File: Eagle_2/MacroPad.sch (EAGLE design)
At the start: 40 parts, among them SW00 SWITCH-SMD-EVQP-P2602W, SW01 KEYSWITCH-PLAIN-MX-1U, SW02 KEYSWITCH-PLAIN-MX-1U, SW03 KEYSWITCH-PLAIN-MX-1U, SW04 KEYSWITCH-PLAIN-MX-1U, SW05 KEYSWITCH-PLAIN-MX-1U, SW06 KEYSWITCH-PLAIN-MX-1U, SW07 KEYSWITCH-PLAIN-MX-1U, SW08 KEYSWITCH-PLAIN-MX-1U, SW09 KEYSWITCH-PLAIN-MX-1U, SW10 KEYSWITCH-PLAIN-MX-1U, SW11 KEYSWITCH-PLAIN-MX-1U, SW12 KEYSWITCH-PLAIN-MX-1U

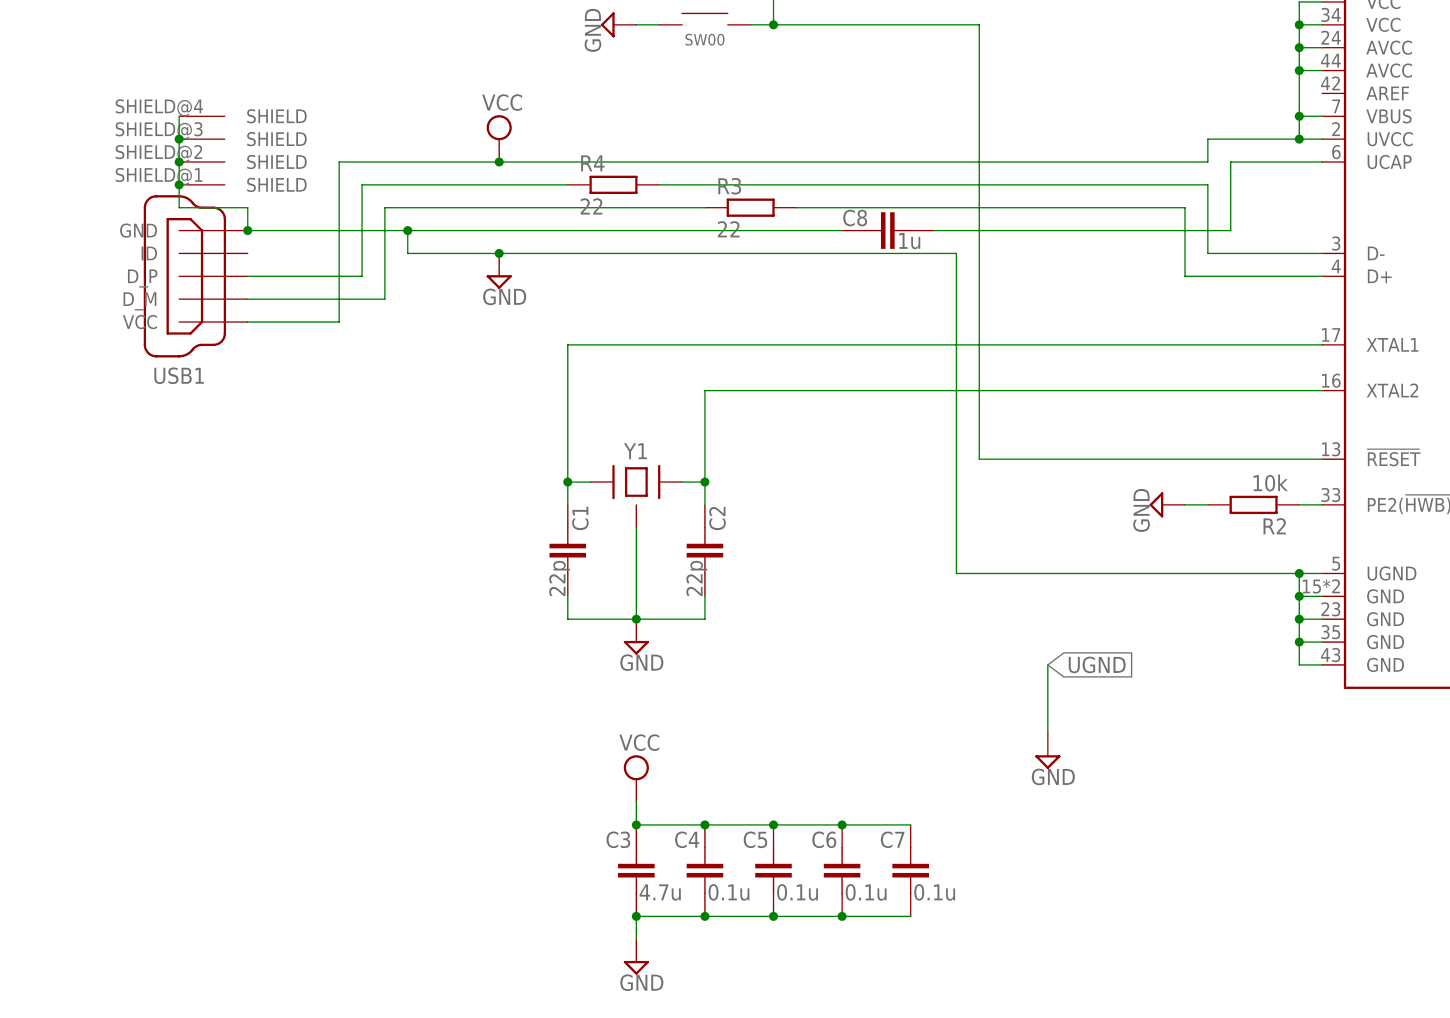
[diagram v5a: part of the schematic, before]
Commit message: Redone schematic with smaller capacitors, fixed decoupling capacitors, and adjusted trace sizes
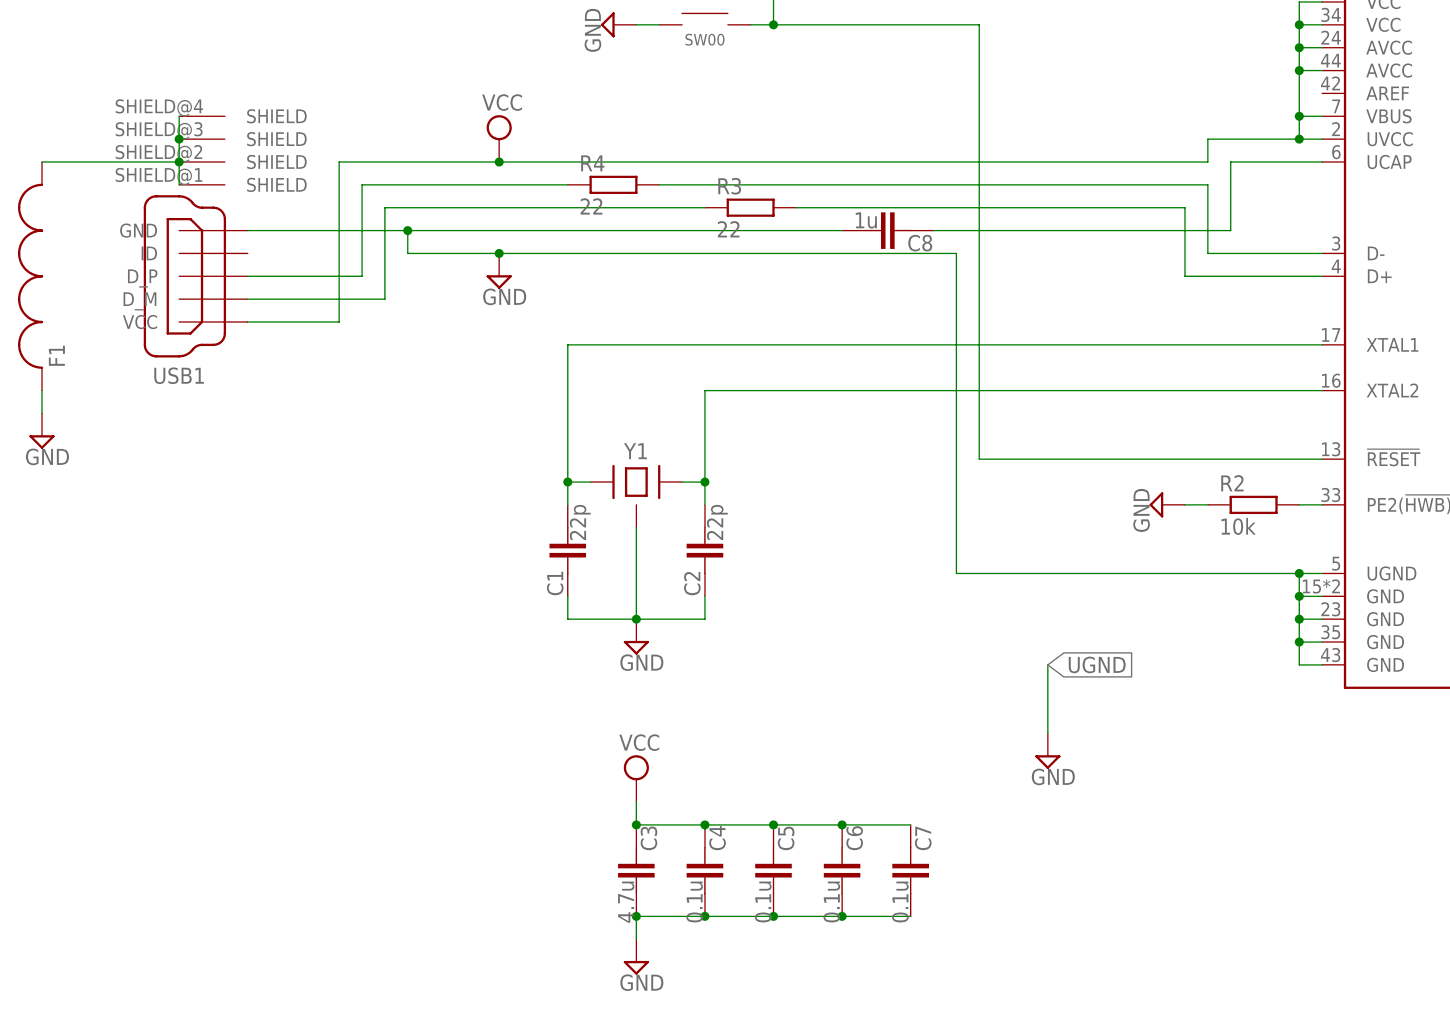
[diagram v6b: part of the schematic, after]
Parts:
- added F1: (no value), USB:FERRITE-0805
- C1, C2, C3, C4, C5, C6, C7, C8: device Components:CAPACITOR-C0805 -> Components:CAPACITOR-0603
- R1, R2, R3, R4: device Components:RESISTOR-0805 -> Components:RESISTOR-0603
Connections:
- new net GND: F1.P$1
- new net N$11: F1.P$2, USB1.SHIELD@1, USB1.SHIELD@2, USB1.SHIELD@3, USB1.SHIELD@4
- net N$1: now also C2.2; no longer C2.1
- net N$2: now also C1.2; no longer C1.1
- net N$4: now also R2.2; no longer R2.1
- net UCAP: now also C8.1; no longer C8.2
- net UGND: now also C1.1, C2.1, C3.2, C4.2, C5.2, C6.2, C7.2, C8.2, R2.1; no longer C1.2, C2.2, C3.1, C4.1, C5.1, C6.1, C7.1, C8.1, R2.2, USB1.SHIELD@1, USB1.SHIELD@2, USB1.SHIELD@3, USB1.SHIELD@4
- net VCC: now also C3.1, C4.1, C5.1, C6.1, C7.1; no longer C3.2, C4.2, C5.2, C6.2, C7.2
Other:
- moved on the sheet: C1, C2, C3, C4, C5, C6, C7, C8, R2

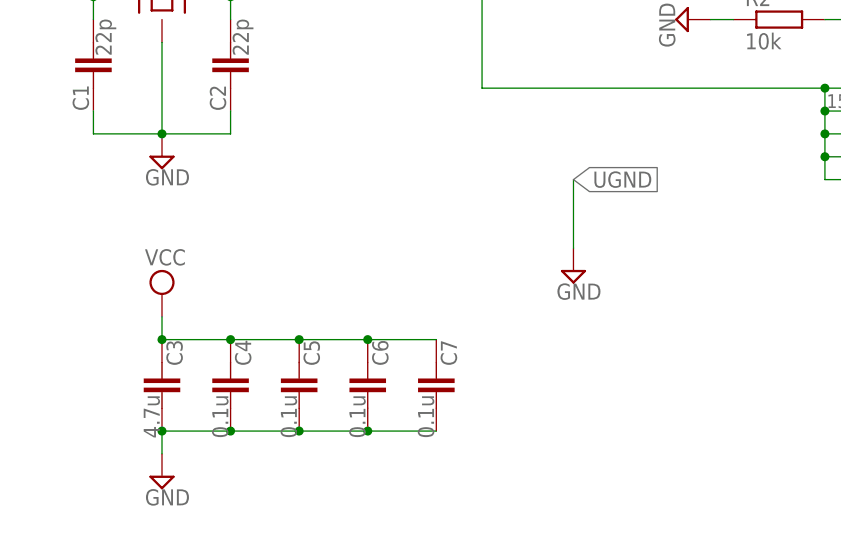
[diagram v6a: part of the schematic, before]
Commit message: Add top and bottom ground plane and merge gnd and ugnd
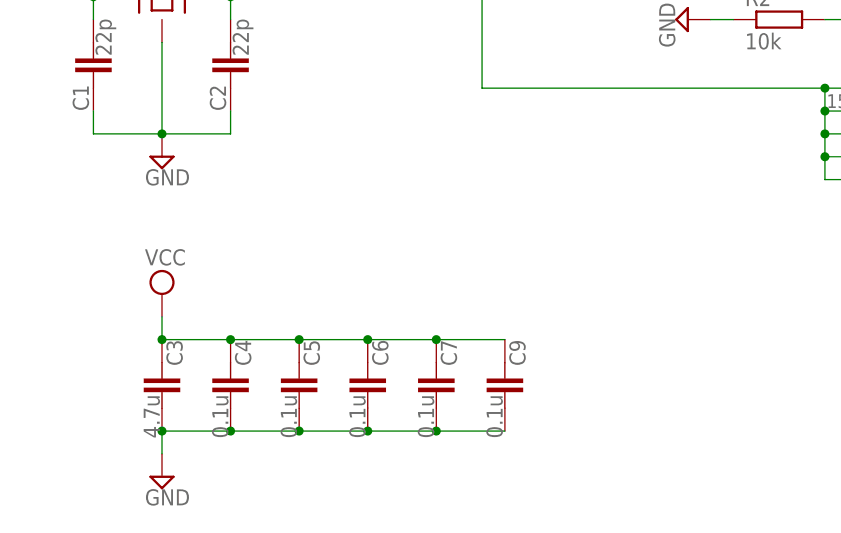
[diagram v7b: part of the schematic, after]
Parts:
- added C9: 0.1u, Components:CAPACITOR-0603
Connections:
- removed net UGND: C1.1, C2.1, C3.2, C4.2, C5.2, C6.2, C7.2, C8.2, R2.1, SW00.1, U$1.GND@15, U$1.GND@23, U$1.GND@35, U$1.GND@43, U$1.UGND, USB1.GND, Y1.GND
- net GND: now also C1.1, C2.1, C3.2, C4.2, C5.2, C6.2, C7.2, C8.2, C9.2, R2.1, SW00.1, U$1.GND@15, U$1.GND@23, U$1.GND@35, U$1.GND@43, U$1.UGND, USB1.GND, Y1.GND
- net VCC: now also C9.1

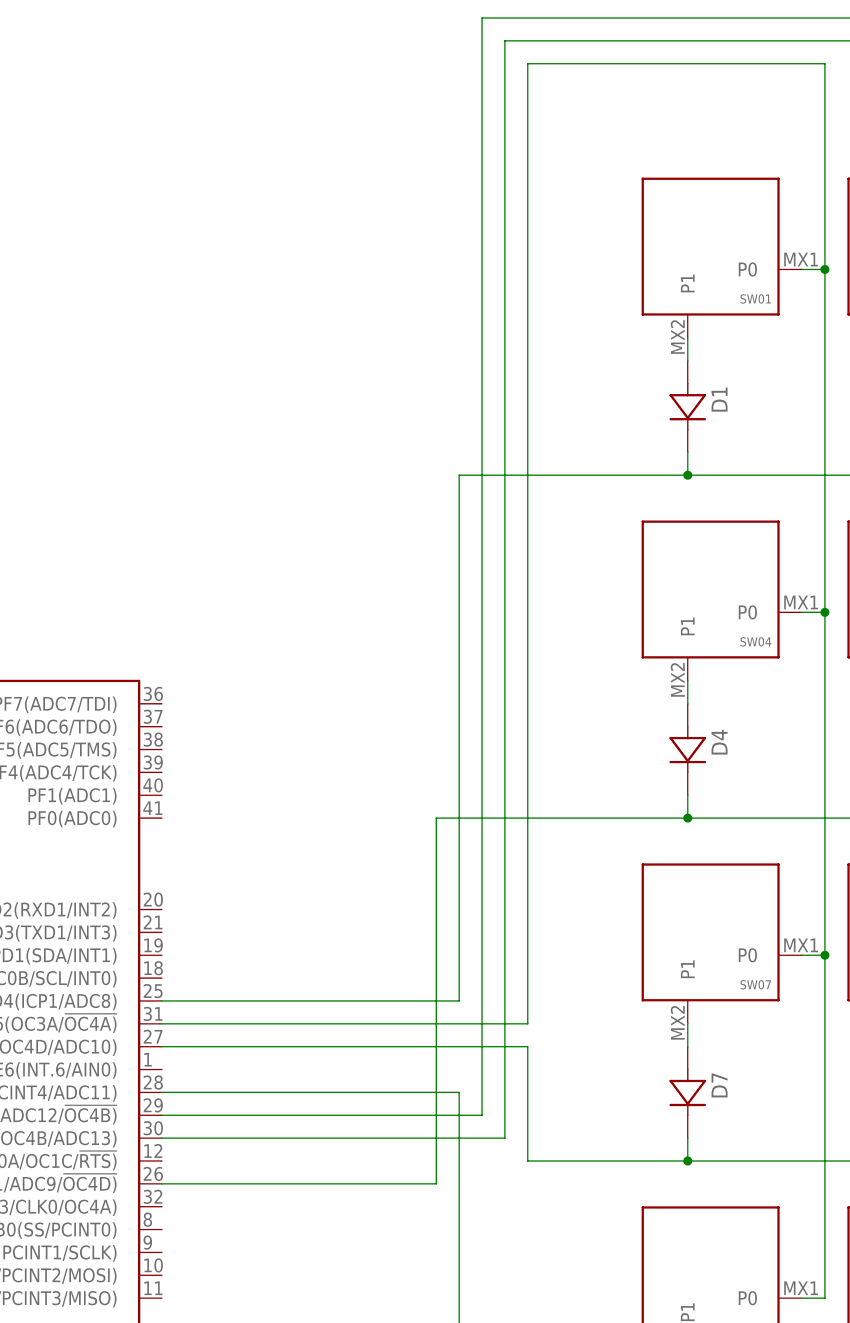
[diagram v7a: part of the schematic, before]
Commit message: Update layout with appropriate spacing between switches (100mil border)
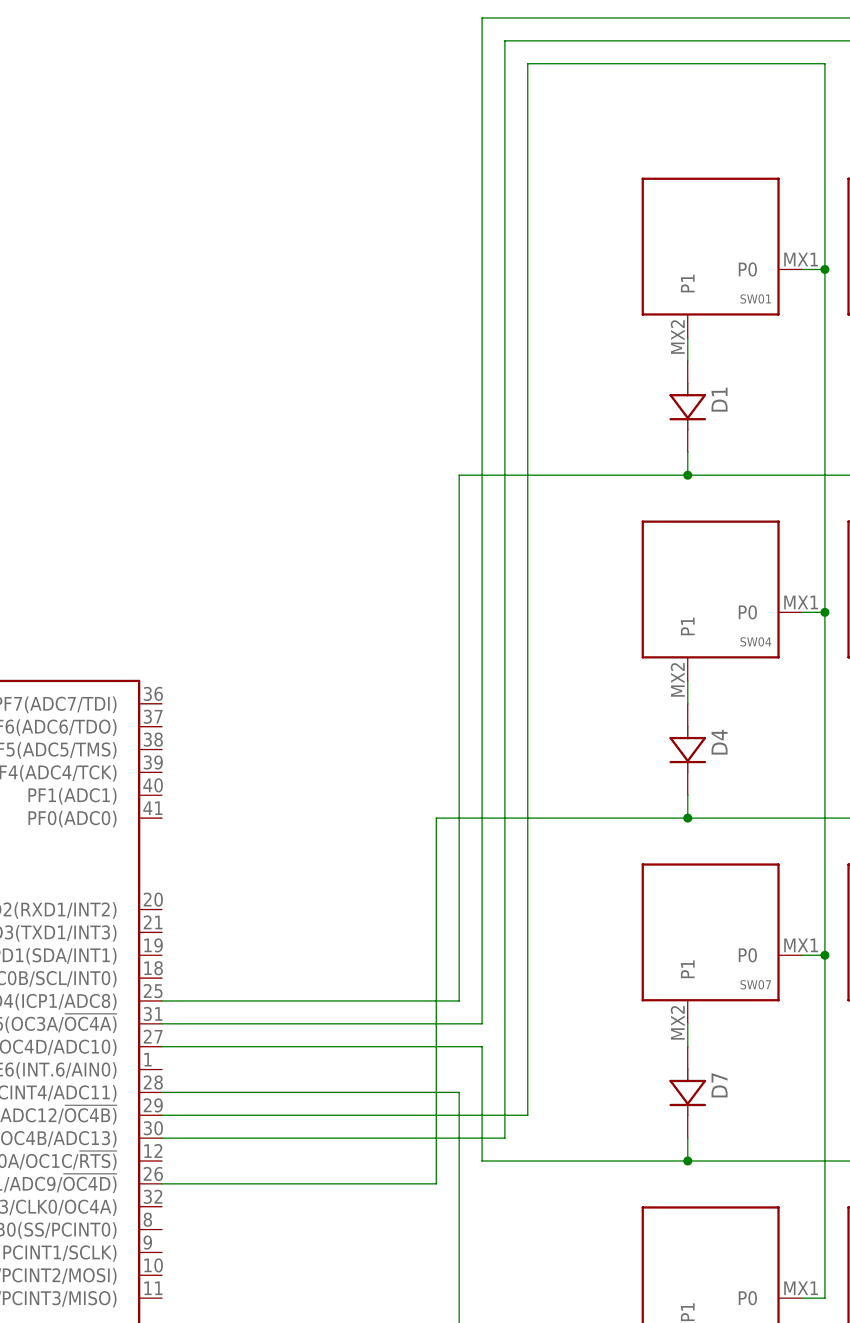
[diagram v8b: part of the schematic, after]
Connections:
- net N$10: now also U$1.PB5(PCINT5/OC1A/ADC12/!OC4B); no longer U$1.PC6(OC3A/!OC4A)
- net N$16: now also U$1.PC6(OC3A/!OC4A); no longer U$1.PB5(PCINT5/OC1A/ADC12/!OC4B)
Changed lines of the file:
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@@
 <junction x="228.6" y="73.66"/>
 <wire x1="195.58" y1="172.72" x2="228.6" y2="172.72" width="0.1524" layer="91"/>
-<pinref part="U$1" gate="G$1" pin="PC6(OC3A/!OC4A)"/>
-<wire x1="154.94" y1="66.04" x2="195.58" y2="66.04" width="0.1524" layer="91"/>
-<wire x1="195.58" y1="66.04" x2="195.58" y2="172.72" width="0.1524" layer="91"/>
+<wire x1="195.58" y1="55.88" x2="195.58" y2="172.72" width="0.1524" layer="91"/>
+<pinref part="U$1" gate="G$1" pin="PB5(PCINT5/OC1A/ADC12/!OC4B)"/>
+<wire x1="154.94" y1="55.88" x2="195.58" y2="55.88" width="0.1524" layer="91"/>
 </segment>
 </net>
@@
 <junction x="274.32" y="73.66"/>
 <wire x1="190.5" y1="177.8" x2="274.32" y2="177.8" width="0.1524" layer="91"/>
-<wire x1="190.5" y1="177.8" x2="190.5" y2="55.88" width="0.1524" layer="91"/>
-<pinref part="U$1" gate="G$1" pin="PB5(PCINT5/OC1A/ADC12/!OC4B)"/>
-<wire x1="190.5" y1="55.88" x2="154.94" y2="55.88" width="0.1524" layer="91"/>
+<wire x1="190.5" y1="177.8" x2="190.5" y2="66.04" width="0.1524" layer="91"/>
+<pinref part="U$1" gate="G$1" pin="PC6(OC3A/!OC4A)"/>
+<wire x1="190.5" y1="66.04" x2="154.94" y2="66.04" width="0.1524" layer="91"/>
 </segment>
 </net>
@@
 <wire x1="236.22" y1="50.8" x2="213.36" y2="50.8" width="0.1524" layer="91"/>
 <junction x="213.36" y="50.8"/>
-<wire x1="213.36" y1="50.8" x2="195.58" y2="50.8" width="0.1524" layer="91"/>
-<wire x1="195.58" y1="50.8" x2="195.58" y2="63.5" width="0.1524" layer="91"/>
+<wire x1="213.36" y1="50.8" x2="190.5" y2="50.8" width="0.1524" layer="91"/>
+<wire x1="190.5" y1="50.8" x2="190.5" y2="63.5" width="0.1524" layer="91"/>
 <pinref part="U$1" gate="G$1" pin="PD7(T0/OC4D/ADC10)"/>
-<wire x1="195.58" y1="63.5" x2="154.94" y2="63.5" width="0.1524" layer="91"/>
+<wire x1="190.5" y1="63.5" x2="154.94" y2="63.5" width="0.1524" layer="91"/>
 </segment>
 </net>
